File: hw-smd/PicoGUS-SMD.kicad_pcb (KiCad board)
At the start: 2 copper layers, 103.7 x 99.8 mm, 81 parts, among them J1 2x9 header, J3 Bus_ISA_8bit, J5 SJ1-3535NG (black), J6 1x40 breakaway header, J7 1x40 breakaway header, J8 SJ1-3535NG-GR (green), J9 Waveblaster 2x13 male, U1 Raspberry Pi Pico, U10 74LVC2G06, U11 NE5532, U12 74LVC2G06, U2 74LVC244, U3 SN74CB3T3257, U4 SN74CB3T3257, U5 74AHC14, U6 74LVC00, U7 74LVC1G00, U8 APS6404L-3SQR-SN, U9 PCM5100A

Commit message: WIP hw-smd: GY-PCM5102 module option (J10) - routing not finished
- Schematic: J10 on the DAC sheet as on the THT board (outputs to AUDIO_L/R,
  leave out U9, C12-C20, FB3, R7, R8 when the module is fitted); ERC 0 errors.
- Board: J10 placed where it is on the THT board, colliding tracks removed.
  0 DRC errors but 17 connections still unrouted - do not order from this commit.
- BOM notes and README DAC-option section.

Co-Authored-By: Claude Opus 5.5 <noreply@anthropic.com>
Claude-Session: https://claude.ai/code/session_011utN3x8yYUNDvkpGCEq5yD
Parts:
- added J10: GY-PCM5102, PiGUS library:GY-PCM5102_Module, F.Cu at (166.2, 75.0)
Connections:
- net Net-(U9-OUTL) renamed /PCM5100 audio/DAC_OUTL
- net Net-(U9-OUTR) renamed /PCM5100 audio/DAC_OUTR
- J3 pad 11: (no net) -> unconnected-(J3-~{SMEMW}-Pad11)
- J3 pad 12: (no net) -> unconnected-(J3-~{SMEMR}-Pad12)
- J3 pad 19: (no net) -> unconnected-(J3-~{DACK0}-Pad19)
- J3 pad 20: (no net) -> unconnected-(J3-CLK-Pad20)
- J3 pad 22: (no net) -> unconnected-(J3-IRQ6-Pad22)
- J3 pad 26: (no net) -> unconnected-(J3-~{DACK2}-Pad26)
- J3 pad 28: (no net) -> unconnected-(J3-ALE-Pad28)
- J3 pad 30: (no net) -> unconnected-(J3-OSC-Pad30)
- J3 pad 32: (no net) -> unconnected-(J3-IO-Pad32)
- J3 pad 43: (no net) -> unconnected-(J3-BA19-Pad43)
- J3 pad 44: (no net) -> unconnected-(J3-BA18-Pad44)
- J3 pad 45: (no net) -> unconnected-(J3-BA17-Pad45)
- J3 pad 46: (no net) -> unconnected-(J3-BA16-Pad46)
- J3 pad 47: (no net) -> unconnected-(J3-BA15-Pad47)
- J3 pad 48: (no net) -> unconnected-(J3-BA14-Pad48)
- J3 pad 49: (no net) -> unconnected-(J3-BA13-Pad49)
- J3 pad 5: (no net) -> unconnected-(J3--5V-Pad5)
- J3 pad 50: (no net) -> unconnected-(J3-BA12-Pad50)
- J3 pad 51: (no net) -> unconnected-(J3-BA11-Pad51)
- J3 pad 52: (no net) -> unconnected-(J3-BA10-Pad52)
- J3 pad 6: (no net) -> unconnected-(J3-DRQ2-Pad6)
- J3 pad 8: (no net) -> unconnected-(J3-UNUSED-Pad8)
- J5 pad RN: (no net) -> unconnected-(J5-PadRN)
- J5 pad TN: (no net) -> unconnected-(J5-PadTN)
- J9 pad 12: (no net) -> unconnected-(J9-Pin_12-Pad12)
- J9 pad 13: (no net) -> unconnected-(J9-Pin_13-Pad13)
- J9 pad 16: (no net) -> unconnected-(J9-Pin_16-Pad16)
- J9 pad 2: (no net) -> unconnected-(J9-Pin_2-Pad2)
- J9 pad 8: (no net) -> unconnected-(J9-Pin_8-Pad8)
- U1 pad 35: (no net) -> unconnected-(U1-ADC_VREF-Pad35)
- U1 pad 37: (no net) -> unconnected-(U1-3V3_EN-Pad37)
- U1 pad 41: (no net) -> unconnected-(U1-SWCLK-Pad41)
- U1 pad 43: (no net) -> unconnected-(U1-SWDIO-Pad43)
- U2 pad 16: (no net) -> unconnected-(U2-1Y1-Pad16)
- U2 pad 7: (no net) -> unconnected-(U2-2Y2-Pad7)
- U2 pad 9: (no net) -> unconnected-(U2-2Y3-Pad9)
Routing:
- net -12V: track 137.0 -> 51.0 mm
- net +5V: track 278.8 -> 215.7 mm
- net /PCM5100 audio/AUDIO_R: track 52.6 -> 0.00 mm, vias 2 -> 0
- net +3V3: track 327.4 -> 276.6 mm
- net /PCM5100 audio/AUDIO_L: track 31.9 -> 0.00 mm
- net LRCK: track 26.0 -> 2.82 mm
- net RUN: track 85.0 -> 72.7 mm
- net UART_TX: track 110.6 -> 99.0 mm

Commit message: hw-smd: J10 module option routed; DAC heading; new back artwork
- All connections routed after adding J10 (autorouter + grid router for the
  stragglers; some long staircase tracks, e.g. -12V and UART_TX, are left for
  the planned re-arrangement). Dangling stubs/vias removed.
  0 DRC errors, 0 unconnected, schematic parity OK.
- "DAC -OR- GY-PCM5102" heading; J10 outline covers the DAC parts.
- Back: new PicoGUS artwork at the same spot as on the THT board; dedication
  still at its previous position (THT has it at 139.5, 60.5).
- Not yet regenerated: BOM-SMD.csv / DigiKey CSVs, README art paragraph,
  schematic PDF, JLCPCB files.

Co-Authored-By: Claude Opus 5.5 <noreply@anthropic.com>
Claude-Session: https://claude.ai/code/session_011utN3x8yYUNDvkpGCEq5yD
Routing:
- net -12V: track 51.0 -> 131.8 mm, vias 2 -> 6
- net +5V: track 215.7 -> 285.8 mm, vias 3 -> 7
- net +3V3: track 276.6 -> 339.9 mm, vias 6 -> 15
- net /PCM5100 audio/AUDIO_R: track 0.00 -> 60.9 mm, vias 0 -> 5
- net /PCM5100 audio/AUDIO_L: track 0.00 -> 46.7 mm, vias 0 -> 7
- net LRCK: track 2.82 -> 32.9 mm
- net UART_TX: track 99.0 -> 121.3 mm, vias 5 -> 9
- net RUN: track 72.7 -> 86.1 mm
- net BCK: track 20.6 -> 29.3 mm
- net DIN: track 19.5 -> 27.4 mm
- net GND: vias 99 -> 112
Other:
- board text added: "DAC -OR- GY-PCM5102"

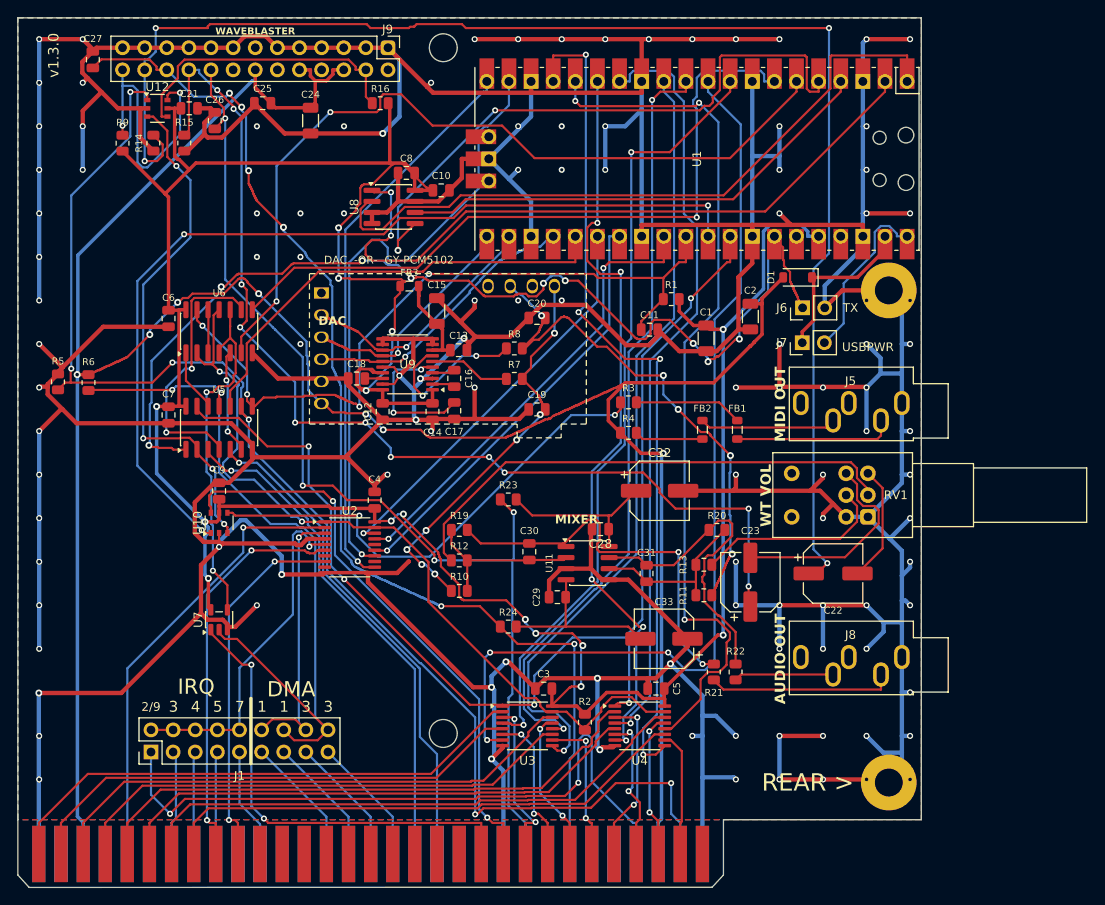
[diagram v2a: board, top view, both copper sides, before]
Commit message: hw-smd: adopt the new component placement; full re-route; new back artwork
- Placement from the updated board (62 of 82 parts moved, all circuit groups).
  Sanity check: no courtyard overlaps; J10 still covers exactly the DAC parts
  (U9, C12-C20, FB3, R7, R8); C32 (7.7 mm) now under the Waveblaster area,
  ~3 mm below a daughterboard; J9 0.67 mm left of its THT position.
- Full re-route from scratch (autorouter, then grid router for the last
  signals: RA8/RA9, ~IOR, DACK, AD7, GND stitching of C9, U9 pins 3/19 and the
  J3 GND finger). 0 DRC errors, 0 unconnected, schematic parity OK.
- Labels on pads / overlapping moved to free spots (angle kept): C2, C10, C14,
  C15, C26, C27, C32, C33, R19; "DAC" off J10 pin 2; "MIXER" off R11/R13.
- Back: new PicoGUS artwork centred over the dedication at its new spot.
- BOM-SMD.csv regenerated with the J10 option (no DigiKey link for the module).

Co-Authored-By: Claude Opus 5.5 <noreply@anthropic.com>
Claude-Session: https://claude.ai/code/session_011utN3x8yYUNDvkpGCEq5yD
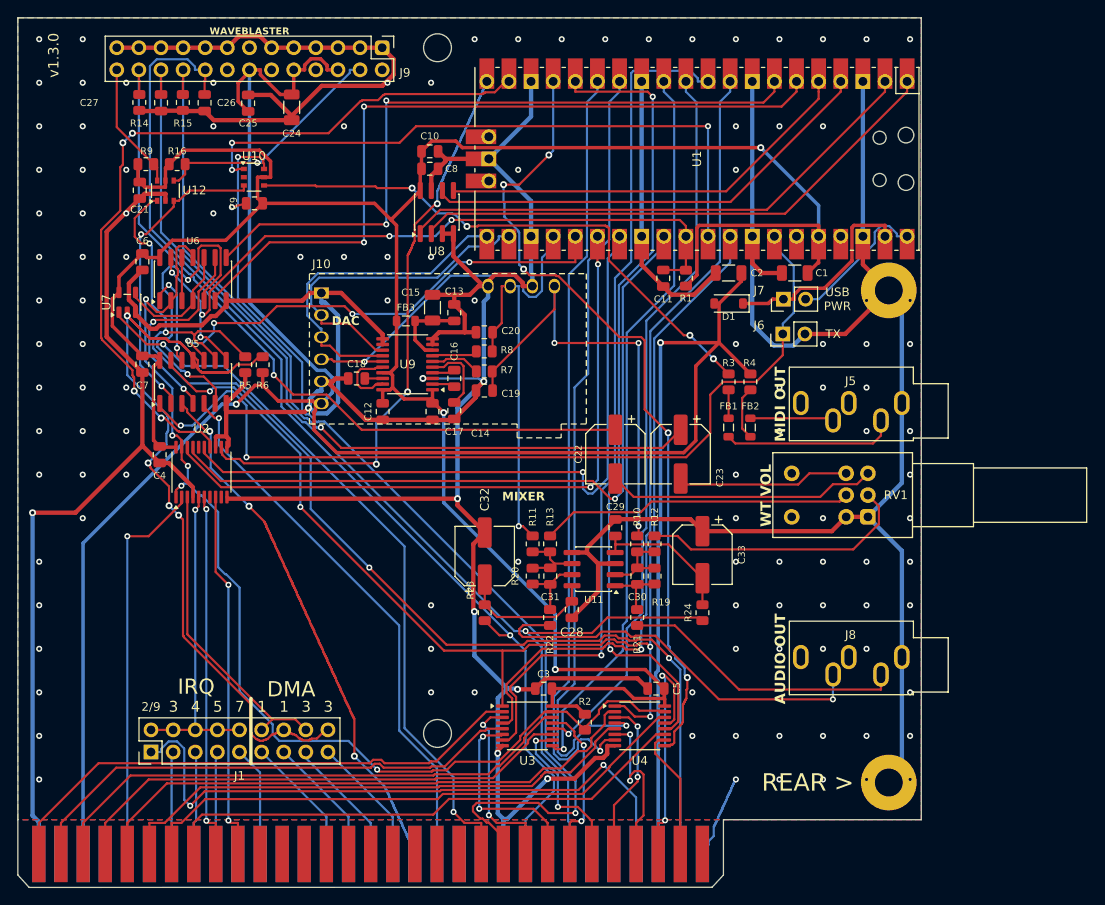
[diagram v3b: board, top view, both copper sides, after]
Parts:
- moved U10 39.9 mm to (143.5, 54.5), turned to 0 degrees
- moved U7 37.9 mm to (128.9, 68.9)
- moved C9 33.3 mm to (143.6, 57.5), turned to 180 degrees
- moved C22 28.5 mm to (185.0, 86.3), turned to -90 degrees
- moved C4 25.2 mm to (132.7, 86.4), turned to -90 degrees
- moved R16 24.3 mm to (134.7, 53.0), turned to 0 degrees
- moved R19 23.0 mm to (189.5, 100.3), turned to -90 degrees
- moved R12 22.5 mm to (189.5, 96.6), turned to -90 degrees
- moved R24 22.4 mm to (195.0, 104.5), turned to 90 degrees
- moved R22 22.2 mm to (177.5, 105.1)
- moved R20 21.8 mm to (175.5, 100.3), turned to -90 degrees
- moved R5 21.6 mm to (142.5, 76.0), turned to -90 degrees
- moved C32 21.4 mm to (170.0, 98.0), turned to 90 degrees
- moved R10 21.1 mm to (187.5, 96.6), turned to -90 degrees
- moved R11 20.5 mm to (175.5, 96.6), turned to -90 degrees
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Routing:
- net GND: track 1103.3 -> 734.9 mm, vias 112 -> 123
- net /Wavetable & line out/WT_L: track 164.8 -> 86.2 mm, vias 4 -> 1
- net +3V3: track 339.9 -> 280.4 mm, vias 15 -> 3
- net I/OCHRDY: track 66.3 -> 115.9 mm
- net Net-(C30-Pad2): track 45.5 -> 7.40 mm, vias 2 -> 0
- net /Wavetable & line out/LINE_R: track 11.9 -> 46.9 mm, vias 0 -> 1
- net ~{BUSOE}: track 92.4 -> 125.5 mm, vias 2 -> 5
- net ~{RI/OCHRDY}: track 105.5 -> 72.6 mm
- net RTC: track 46.7 -> 77.8 mm, vias 1 -> 2
- net AEN: track 53.5 -> 84.3 mm
- net RDRQ: track 53.1 -> 83.8 mm, vias 2 -> 1
- net RIRQ: track 49.3 -> 79.1 mm
- net /Wavetable & line out/WT_R: track 123.0 -> 94.1 mm, vias 11 -> 1
- net Net-(C31-Pad2): track 36.3 -> 7.91 mm
- net Net-(R12-Pad1): track 58.8 -> 31.4 mm
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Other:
- board text added: "USB PWR"
- board text removed: "DAC -OR- GY-PCM5102"
- board text removed: "USBPWR"

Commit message: Mixer: +6 dB Waveblaster gain (R10/R11/R19/R20 20k, C30/C31 47p)
Waveblaster daughterboards put out about 1-1.2 Vrms full scale (DreamBlaster X2:
AK4388, 1.13 Vrms) against the PCM5100A's 2.1 Vrms, so with unity WT gain MIDI
was 5-6 dB quieter than PCM at RV1 max.

Raise the summer's feedback and PCM input resistors from 10k to 20k on both
boards: WT gain at RV1 max = 20k/10k = 2 (+6 dB), PCM 20k/20.47k (-0.2 dB, as
before). The daughterboard load (about 4.8k at RV1 max) and the pot taper stay
unchanged. C30/C31 100p -> 47p keeps the feedback pole at ~170 kHz.

BOM-only change (no copper change): schematic values/fields, PCB values,
BOM-THT/BOM-SMD lines with the previous values in the notes, DigiKey upload
files (1x/10x), schematic PDFs. SMD C30/C31 get an LCSC field (C14857,
CL21C470JBANNNC) because DigiKey only stocks the 100 V CL21C470JC61PNC.
README mixer text updated; the THT diagram now shows R14 on the J9 side of C22
and R12 joined to the summing node. ERC 0, DRC 0 with schematic parity.

Co-Authored-By: Claude Opus 5.5 <noreply@anthropic.com>
Claude-Session: https://claude.ai/code/session_011utN3x8yYUNDvkpGCEq5yD
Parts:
- C30, C31: value 100pF C0G -> 47pF C0G
- R10, R11, R19, R20: value 10k -> 20k
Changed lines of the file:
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@@
 			)
 		)
-		(property "Value" "10k"
+		(property "Value" "20k"
 			(at 0 1.65 90)
 			(layer "F.Fab")
@@
 			)
 		)
-		(property "Value" "100pF C0G"
+		(property "Value" "47pF C0G"
 			(at 0 1.68 90)
 			(layer "F.Fab")
@@
 			)
 		)
-		(property "Value" "10k"
+		(property "Value" "20k"
 			(at 0 1.65 90)
 			(layer "F.Fab")
@@
 			)
 		)
-		(property "Value" "10k"
+		(property "Value" "20k"
 			(at 0 1.65 90)
 			(layer "F.Fab")
@@
 			)
 		)
-		(property "Value" "10k"
+		(property "Value" "20k"
 			(at 0 1.65 90)
 			(layer "F.Fab")
@@
 			)
 		)
-		(property "Value" "100pF C0G"
+		(property "Value" "47pF C0G"
 			(at 0 1.68 90)
 			(layer "F.Fab")
